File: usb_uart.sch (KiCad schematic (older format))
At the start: 12 parts, among them U20 CP2102N-A01-GQFN28, U25 CM1293A-04SO

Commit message: Fixed USB micro-b's mount polarity; Improved SOT-23-6 1-pin silk marker readability
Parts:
- U25: footprint TO_SOT_Packages_SMD:SOT-23-6_Handsoldering -> components:SOT-23-6_Handsoldering_mod
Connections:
- wire segments 75 -> 73
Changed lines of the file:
@@
 	3400 2800 3400 3050
 Wire Wire Line
-	3400 3050 4450 3050
+	3400 3050 3550 3050
 Wire Wire Line
 	4450 3050 4450 2650
@@
 F 0 "U25" H 2950 4328 50  0000 C CNN
 F 1 "CM1293A-04SO" H 2950 4237 50  0000 C CNN
-F 2 "TO_SOT_Packages_SMD:SOT-23-6_Handsoldering" H 2950 3650 50  0001 C CNN
+F 2 "components:SOT-23-6_Handsoldering_mod" H 2950 3650 50  0001 C CNN
 F 3 "http://www.onsemi.com/pub/Collateral/SRV05-4-D.PDF" H 2950 3650 50  0001 C CNN
 	1    2950 3650
@@
 $EndComp
 Wire Wire Line
-	2450 3100 2450 3550
-Wire Wire Line
-	2600 3050 2400 3050
-Wire Wire Line
-	2400 3050 2400 3750
-Wire Wire Line
-	2400 3750 2450 3750
-Wire Wire Line
-	2450 3100 2650 3100
-Wire Wire Line
 	3300 2850 3300 3150
 Wire Wire Line
@@
 Wire Wire Line
 	2800 2850 3300 2850
-Wire Wire Line
-	2950 4150 3450 4150
-Wire Wire Line
-	3450 4150 3450 3750
-Connection ~ 2950 4150
-Wire Wire Line
-	3450 3750 3450 3550
-Connection ~ 3450 3750
 Text GLabel 6850 1950 2    60   Input ~ 0
 E_TX
@@
 VBUS
 Wire Wire Line
-	2400 2700 2600 2700
-Wire Wire Line
-	2400 2800 2650 2800
-Wire Wire Line
-	2600 3050 2600 2700
-Connection ~ 2600 2700
-Wire Wire Line
-	2600 2700 3450 2700
-Wire Wire Line
-	2650 3100 2650 2800
-Connection ~ 2650 2800
-Wire Wire Line
-	2650 2800 3400 2800
+	2400 2800 3400 2800
+Wire Wire Line
+	2400 2700 2450 2700
+Wire Wire Line
+	3550 3050 3550 3750
+Wire Wire Line
+	3550 3750 3450 3750
+Connection ~ 3550 3050
+Wire Wire Line
+	3550 3050 4450 3050
+Wire Wire Line
+	2450 3550 2450 2700
+Connection ~ 2450 2700
+Wire Wire Line
+	2450 2700 3450 2700
+Connection ~ 2950 4150
+Wire Wire Line
+	2950 4150 2450 4150
+Wire Wire Line
+	2450 4150 2450 3750
+Wire Wire Line
+	3450 3550 3500 3550
+Wire Wire Line
+	3500 3550 3500 4150
+Wire Wire Line
+	2950 4150 3500 4150
 $EndSCHEMATC

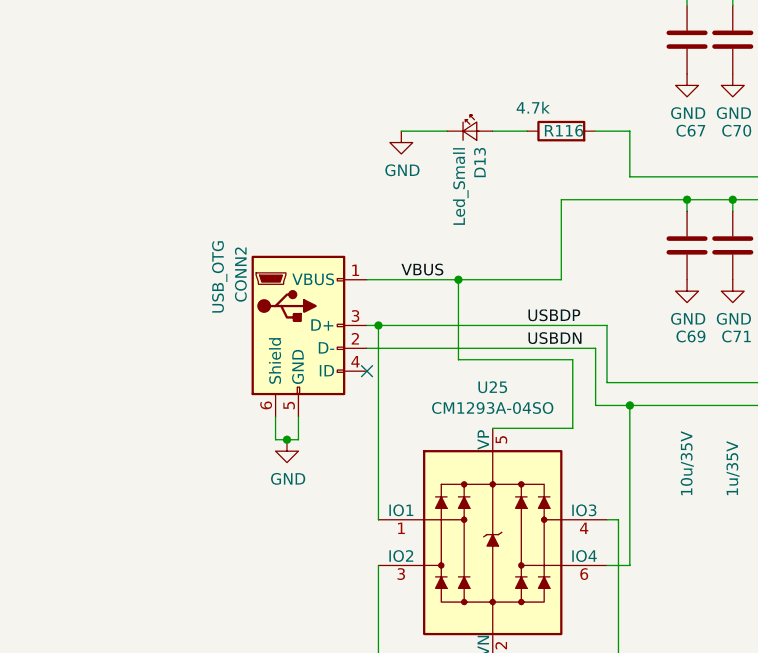
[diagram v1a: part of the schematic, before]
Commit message: Added 4-pin USB pin header connector in case of getting crazy of USB micro-B comming off
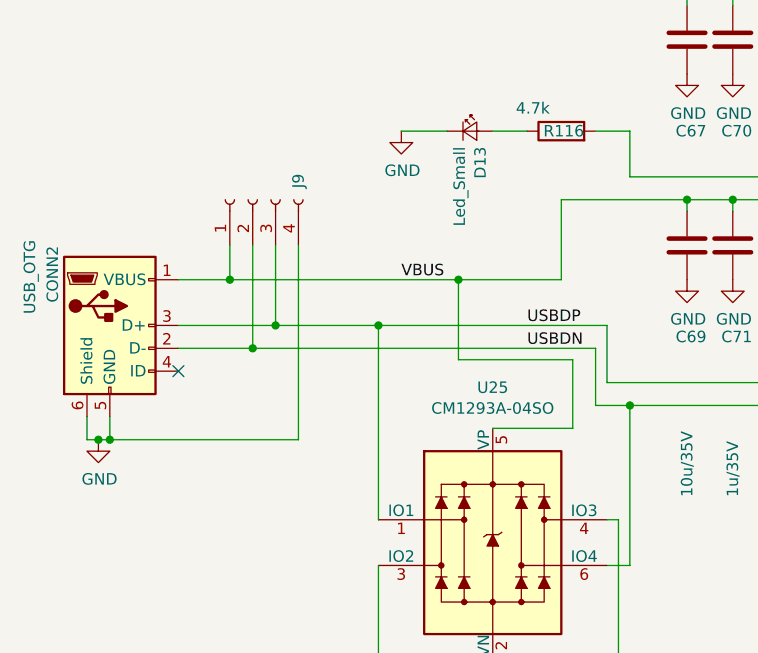
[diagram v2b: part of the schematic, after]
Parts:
- added J9: Conn_01x04_Female, Connector_PinHeader_2.54mm:PinHeader_1x04_P2.54mm_Vertical, symbol dotmatrix_64x48-rescue:Conn_01x04_Female-Connector
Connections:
- wire segments 73 -> 81
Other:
- moved on the sheet: CONN2
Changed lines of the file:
@@
 L dotmatrix_64x48-rescue:USB_OTG-Connector CONN?
 U 1 1 5BBED423
-P 2100 2700
+P 1275 2700
 AR Path="/584C83E3/5BBED423" Ref="CONN?"  Part="1"
 AR Path="/5BBED423" Ref="CONN?"  Part="1"
 AR Path="/5BB33F0A/5BBED423" Ref="CONN2"  Part="1"
-F 0 "CONN2" V 1850 2800 50  0000 L CNN
-F 1 "USB_OTG" V 1750 2750 50  0000 L CNN
-F 2 "components:USB_Micro-B_Jing_A01SB141B1-067" V 2086 2888 50  0001 L CNN
-F 3 "" V 2050 2600 50  0000 C CNN
-	1    2100 2700
-	1    0    0    -1
-$EndComp
-Wire Wire Line
-	2000 3200 2000 3100
-Wire Wire Line
-	2100 3200 2100 3100
-NoConn ~ 2400 2900
-Wire Wire Line
-	2000 3200 2050 3200
+F 0 "CONN2" V 1025 2800 50  0000 L CNN
+F 1 "USB_OTG" V 925 2750 50  0000 L CNN
+F 2 "components:USB_Micro-B_Jing_A01SB141B1-067" V 1261 2888 50  0001 L CNN
+F 3 "" V 1225 2600 50  0000 C CNN
+	1    1275 2700
+	1    0    0    -1
+$EndComp
+Wire Wire Line
+	1175 3200 1175 3100
+Wire Wire Line
+	1275 3200 1275 3100
+NoConn ~ 1575 2900
+Wire Wire Line
+	1175 3200 1225 3200
 $Comp
 L dotmatrix_64x48-rescue:GND-power #PWR019
 U 1 1 5BBF16CE
-P 2050 3200
-F 0 "#PWR019" H 2050 2950 50  0001 C CNN
-F 1 "GND" H 2055 3027 50  0000 C CNN
-F 2 "" H 2050 3200 50  0001 C CNN
-F 3 "" H 2050 3200 50  0001 C CNN
-	1    2050 3200
-	1    0    0    -1
-$EndComp
-Connection ~ 2050 3200
-Wire Wire Line
-	2050 3200 2100 3200
+P 1225 3200
+F 0 "#PWR019" H 1225 2950 50  0001 C CNN
+F 1 "GND" H 1230 3027 50  0000 C CNN
+F 2 "" H 1225 3200 50  0001 C CNN
+F 3 "" H 1225 3200 50  0001 C CNN
+	1    1225 3200
+	1    0    0    -1
+$EndComp
+Connection ~ 1225 3200
+Wire Wire Line
+	1225 3200 1275 3200
 Wire Wire Line
 	3250 2500 3250 2150
@@
 Wire Wire Line
 	2800 2500 3250 2500
-Wire Wire Line
-	2800 2500 2400 2500
 Connection ~ 2800 2500
 NoConn ~ 6050 1550
@@
 VBUS
 Wire Wire Line
-	2400 2800 3400 2800
-Wire Wire Line
-	2400 2700 2450 2700
-Wire Wire Line
 	3550 3050 3550 3750
 Wire Wire Line
@@
 Wire Wire Line
 	2950 4150 3500 4150
+$Comp
+L dotmatrix_64x48-rescue:Conn_01x04_Female-Connector J9
+U 1 1 5E1316BB
+P 1900 2150
+F 0 "J9" H 1950 1950 50  0000 L CNN
+F 1 "Conn_01x04_Female" H 1300 1850 50  0001 L CNN
+F 2 "Connector_PinHeader_2.54mm:PinHeader_1x04_P2.54mm_Vertical" H 1900 2150 50  0001 C CNN
+F 3 "" H 1900 2150 50  0001 C CNN
+	1    1900 2150
+	0    -1   -1   0
+$EndComp
+Wire Wire Line
+	1575 2500 1800 2500
+Wire Wire Line
+	1800 2350 1800 2500
+Connection ~ 1800 2500
+Wire Wire Line
+	1800 2500 2800 2500
+Wire Wire Line
+	2100 2350 2100 3200
+Wire Wire Line
+	2100 3200 1275 3200
+Connection ~ 1275 3200
+Wire Wire Line
+	1575 2800 1900 2800
+Wire Wire Line
+	1575 2700 2000 2700
+Wire Wire Line
+	1900 2350 1900 2800
+Connection ~ 1900 2800
+Wire Wire Line
+	1900 2800 3400 2800
+Wire Wire Line
+	2000 2350 2000 2700
+Connection ~ 2000 2700
+Wire Wire Line
+	2000 2700 2450 2700
 $EndSCHEMATC
